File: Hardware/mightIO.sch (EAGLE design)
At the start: 45 parts, among them IC1 TL064D, IC2 TL064D, IC3 LM4041A12DBZ, U1 MAX11612

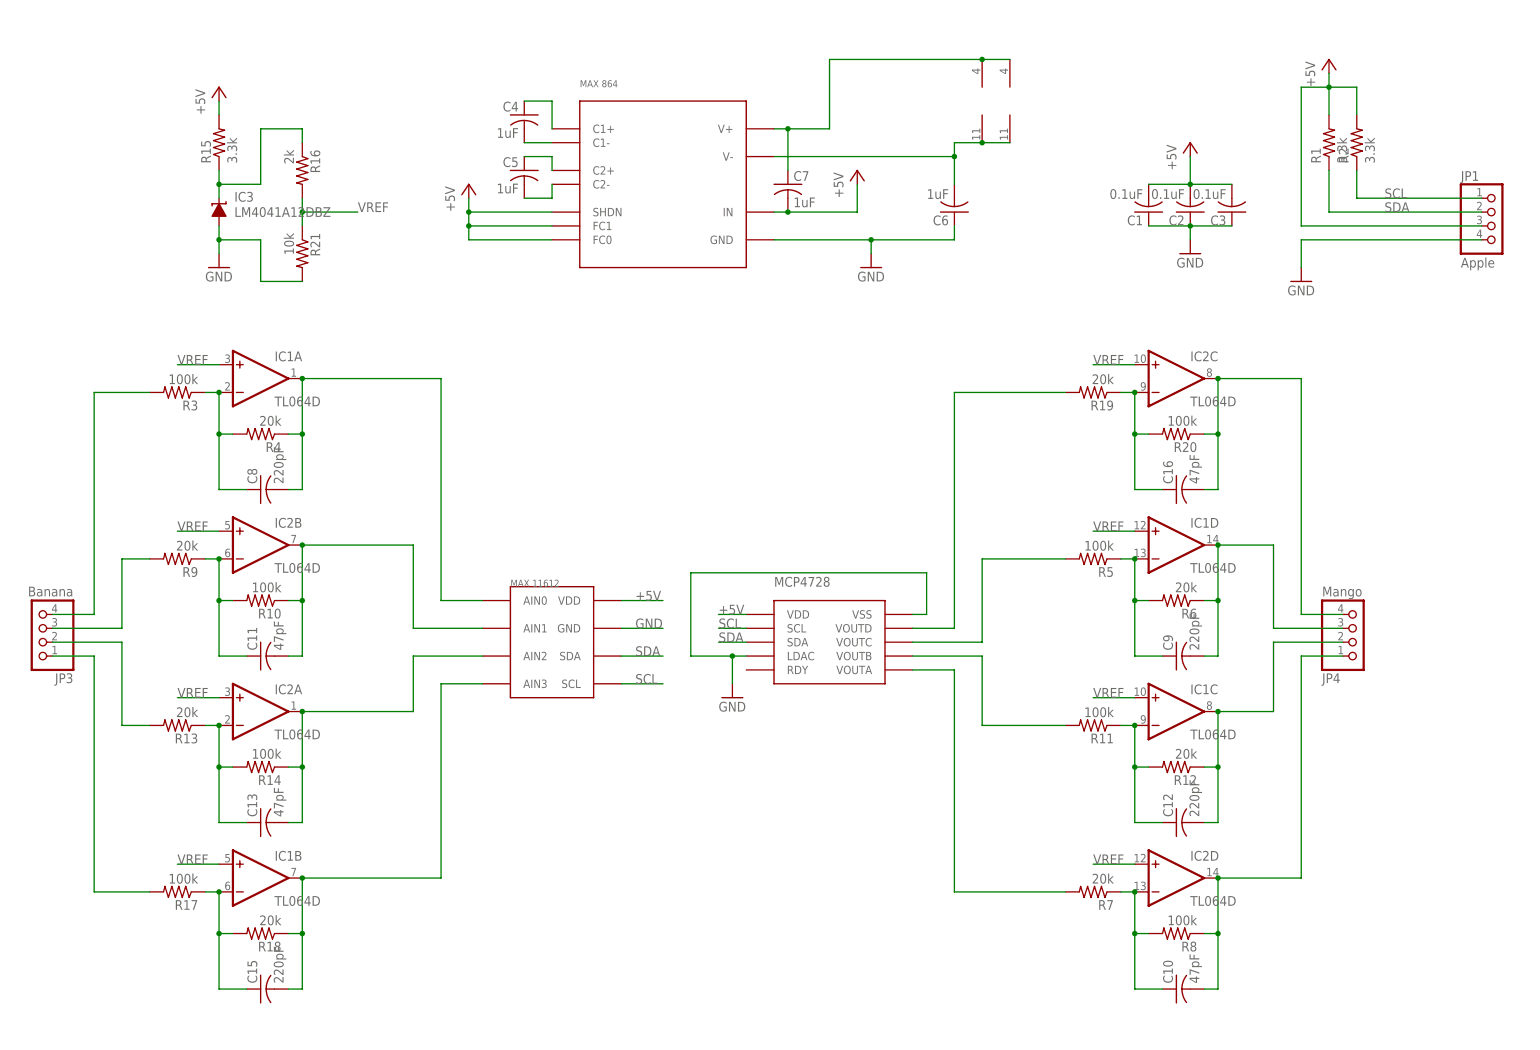
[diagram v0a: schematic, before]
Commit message: Some part value updates
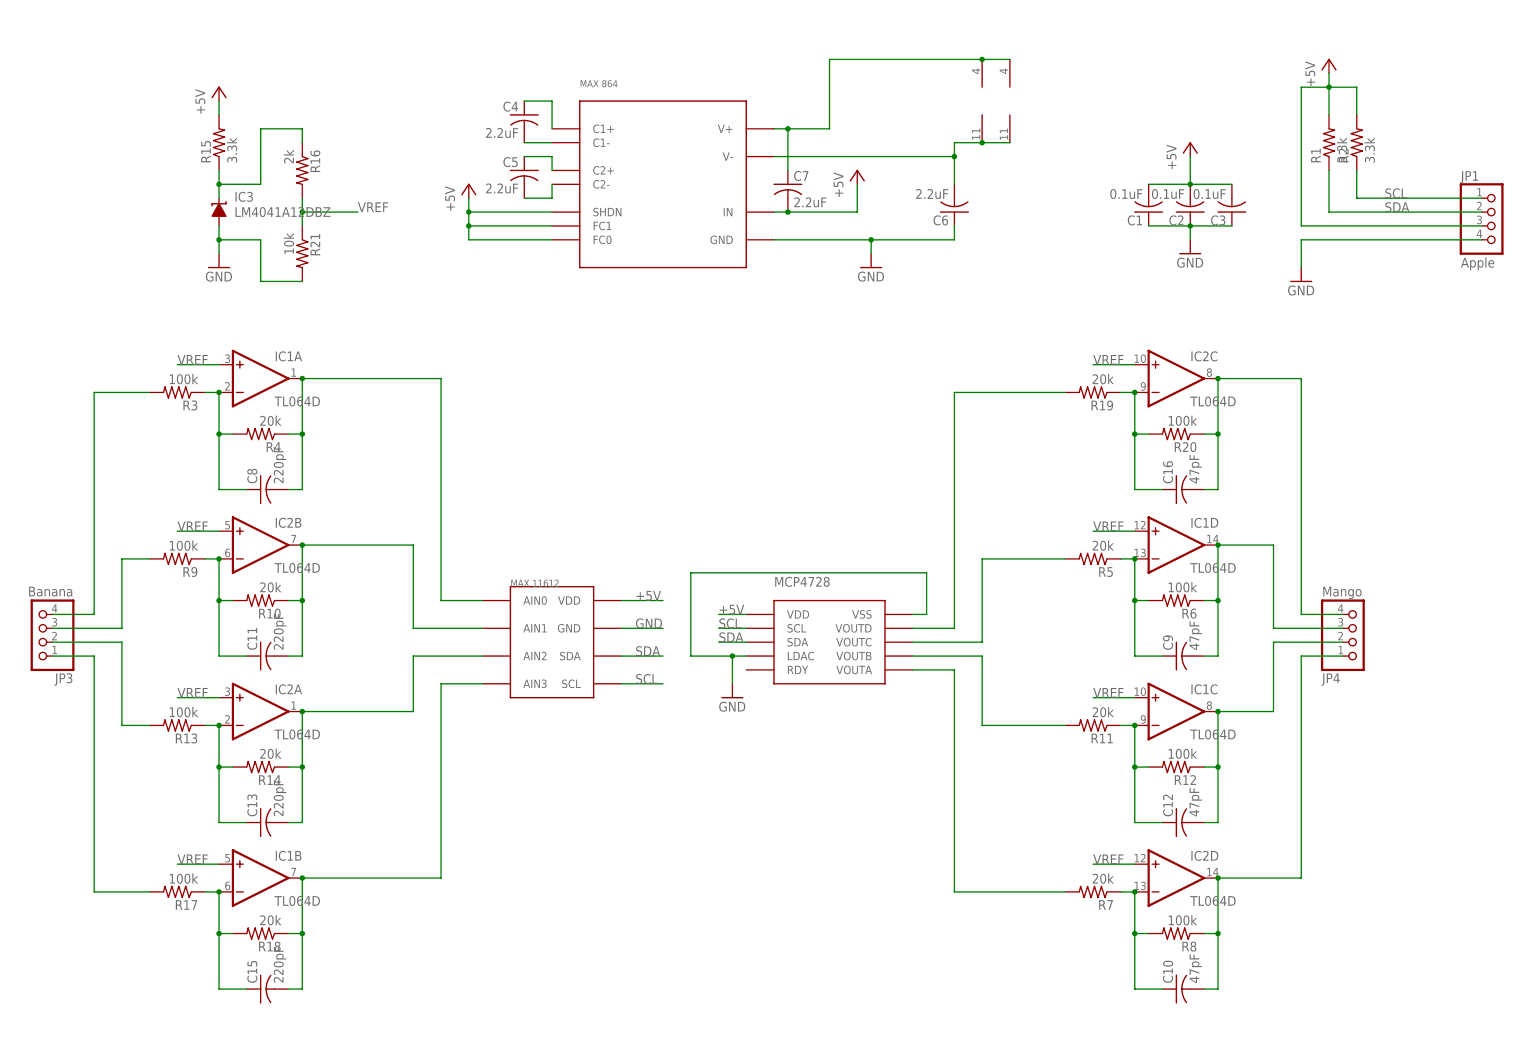
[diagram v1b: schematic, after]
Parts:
- C11, C13: value 47pF -> 220pF
- C12, C9: value 220pF -> 47pF
- C4, C5, C6, C7: value 1uF -> 2.2uF
- R10, R11, R14, R5: value 100k -> 20k
- R12, R13, R6, R9: value 20k -> 100k
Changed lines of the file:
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@@
 <part name="C2" library="rcl" deviceset="C-US" device="C0603" value="0.1uF"/>
 <part name="C3" library="rcl" deviceset="C-US" device="C0603" value="0.1uF"/>
-<part name="C4" library="rcl" deviceset="C-US" device="C0603" value="1uF"/>
-<part name="C5" library="rcl" deviceset="C-US" device="C0603" value="1uF"/>
-<part name="C7" library="rcl" deviceset="C-US" device="C0603" value="1uF"/>
+<part name="C4" library="rcl" deviceset="C-US" device="C0603" value="2.2uF"/>
+<part name="C5" library="rcl" deviceset="C-US" device="C0603" value="2.2uF"/>
+<part name="C7" library="rcl" deviceset="C-US" device="C0603" value="2.2uF"/>
 <part name="P+3" library="supply1" deviceset="+5V" device=""/>
 <part name="P+4" library="supply1" deviceset="+5V" device=""/>
-<part name="C6" library="rcl" deviceset="C-US" device="C0603" value="1uF"/>
+<part name="C6" library="rcl" deviceset="C-US" device="C0603" value="2.2uF"/>
 <part name="IC1" library="linear" deviceset="TL064" device="D"/>
 <part name="IC2" library="linear" deviceset="TL064" device="D"/>
@@
 <part name="R4" library="rcl" deviceset="R-US_" device="R0603" value="20k"/>
 <part name="C8" library="rcl" deviceset="C-US" device="C0603" value="220pF"/>
-<part name="R5" library="rcl" deviceset="R-US_" device="R0603" value="100k"/>
-<part name="R6" library="rcl" deviceset="R-US_" device="R0603" value="20k"/>
-<part name="C9" library="rcl" deviceset="C-US" device="C0603" value="220pF"/>
+<part name="R5" library="rcl" deviceset="R-US_" device="R0603" value="20k"/>
+<part name="R6" library="rcl" deviceset="R-US_" device="R0603" value="100k"/>
+<part name="C9" library="rcl" deviceset="C-US" device="C0603" value="47pF"/>
 <part name="R7" library="rcl" deviceset="R-US_" device="R0603" value="20k"/>
 <part name="R8" library="rcl" deviceset="R-US_" device="R0603" value="100k"/>
 <part name="C10" library="rcl" deviceset="C-US" device="C0603" value="47pF"/>
-<part name="R9" library="rcl" deviceset="R-US_" device="R0603" value="20k"/>
-<part name="R10" library="rcl" deviceset="R-US_" device="R0603" value="100k"/>
-<part name="C11" library="rcl" deviceset="C-US" device="C0603" value="47pF"/>
-<part name="R11" library="rcl" deviceset="R-US_" device="R0603" value="100k"/>
-<part name="R12" library="rcl" deviceset="R-US_" device="R0603" value="20k"/>
-<part name="C12" library="rcl" deviceset="C-US" device="C0603" value="220pF"/>
-<part name="R13" library="rcl" deviceset="R-US_" device="R0603" value="20k"/>
-<part name="R14" library="rcl" deviceset="R-US_" device="R0603" value="100k"/>
-<part name="C13" library="rcl" deviceset="C-US" device="C0603" value="47pF"/>
+<part name="R9" library="rcl" deviceset="R-US_" device="R0603" value="100k"/>
+<part name="R10" library="rcl" deviceset="R-US_" device="R0603" value="20k"/>
+<part name="C11" library="rcl" deviceset="C-US" device="C0603" value="220pF"/>
+<part name="R11" library="rcl" deviceset="R-US_" device="R0603" value="20k"/>
+<part name="R12" library="rcl" deviceset="R-US_" device="R0603" value="100k"/>
+<part name="C12" library="rcl" deviceset="C-US" device="C0603" value="47pF"/>
+<part name="R13" library="rcl" deviceset="R-US_" device="R0603" value="100k"/>
+<part name="R14" library="rcl" deviceset="R-US_" device="R0603" value="20k"/>
+<part name="C13" library="rcl" deviceset="C-US" device="C0603" value="220pF"/>
 <part name="R17" library="rcl" deviceset="R-US_" device="R0603" value="100k"/>
 <part name="R18" library="rcl" deviceset="R-US_" device="R0603" value="20k"/>

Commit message: Some routing updates, more needed
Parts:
- added C14: 0.1uF, rcl:C-USC0603
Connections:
- net GND: now also C14.1
- net VREF: now also C14.2
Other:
- moved on the sheet: IC3, R15, R16, R21
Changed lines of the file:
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@@
 <?xml version="1.0" encoding="utf-8"?>
 <!DOCTYPE eagle SYSTEM "eagle.dtd">
-<eagle version="6.5.0">
+<eagle version="7.0.0">
 <drawing>
 <settings>
@@
 <part name="GND3" library="supply1" deviceset="GND" device=""/>
 <part name="P+1" library="supply1" deviceset="+5V" device=""/>
+<part name="C14" library="rcl" deviceset="C-US" device="C0603" value="0.1uF"/>
 </parts>
 <sheets>
@@
 <instance part="R20" gate="G$1" x="127" y="27.94" rot="R180"/>
 <instance part="C16" gate="G$1" x="127" y="17.78" rot="R90"/>
-<instance part="IC3" gate="G$1" x="-48.26" y="68.58"/>
-<instance part="R15" gate="G$1" x="-48.26" y="81.28" rot="R90"/>
-<instance part="R16" gate="G$1" x="-33.02" y="76.2" rot="R270"/>
-<instance part="R21" gate="G$1" x="-33.02" y="60.96" rot="R270"/>
-<instance part="P+5" gate="1" x="-48.26" y="91.44"/>
-<instance part="GND4" gate="1" x="-48.26" y="58.42"/>
+<instance part="IC3" gate="G$1" x="-63.5" y="71.12"/>
+<instance part="R15" gate="G$1" x="-63.5" y="83.82" rot="R90"/>
+<instance part="R16" gate="G$1" x="-48.26" y="78.74" rot="R270"/>
+<instance part="R21" gate="G$1" x="-48.26" y="63.5" rot="R270"/>
+<instance part="P+5" gate="1" x="-63.5" y="93.98"/>
+<instance part="GND4" gate="1" x="-63.5" y="60.96"/>
 <instance part="JP1" gate="A" x="185.42" y="66.04"/>
 <instance part="GND5" gate="1" x="149.86" y="55.88"/>
@@
 <instance part="GND3" gate="1" x="71.12" y="58.42"/>
 <instance part="P+1" gate="1" x="68.58" y="76.2"/>
+<instance part="C14" gate="G$1" x="-35.56" y="63.5" rot="R180"/>
 </instances>
 <busses>
@@
 <segment>
 <pinref part="IC3" gate="G$1" pin="A"/>
-<wire x1="-48.26" y1="66.04" x2="-48.26" y2="63.5" width="0.1524" layer="91"/>
+<wire x1="-63.5" y1="68.58" x2="-63.5" y2="66.04" width="0.1524" layer="91"/>
 <pinref part="GND4" gate="1" pin="GND"/>
 <pinref part="R21" gate="G$1" pin="2"/>
-<wire x1="-48.26" y1="63.5" x2="-48.26" y2="60.96" width="0.1524" layer="91"/>
-<wire x1="-33.02" y1="55.88" x2="-40.64" y2="55.88" width="0.1524" layer="91"/>
-<wire x1="-40.64" y1="55.88" x2="-40.64" y2="63.5" width="0.1524" layer="91"/>
-<wire x1="-40.64" y1="63.5" x2="-48.26" y2="63.5" width="0.1524" layer="91"/>
-<junction x="-48.26" y="63.5"/>
+<wire x1="-63.5" y1="66.04" x2="-63.5" y2="63.5" width="0.1524" layer="91"/>
+<wire x1="-48.26" y1="58.42" x2="-55.88" y2="58.42" width="0.1524" layer="91"/>
+<wire x1="-55.88" y1="58.42" x2="-55.88" y2="66.04" width="0.1524" layer="91"/>
+<wire x1="-55.88" y1="66.04" x2="-63.5" y2="66.04" width="0.1524" layer="91"/>
+<junction x="-63.5" y="66.04"/>
+<pinref part="C14" gate="G$1" pin="1"/>
+<wire x1="-35.56" y1="60.96" x2="-35.56" y2="58.42" width="0.1524" layer="91"/>
+<wire x1="-35.56" y1="58.42" x2="-48.26" y2="58.42" width="0.1524" layer="91"/>
+<junction x="-48.26" y="58.42"/>
 </segment>
 <segment>
@@
 <pinref part="R15" gate="G$1" pin="2"/>
 <pinref part="P+5" gate="1" pin="+5V"/>
-<wire x1="-48.26" y1="88.9" x2="-48.26" y2="86.36" width="0.1524" layer="91"/>
+<wire x1="-63.5" y1="91.44" x2="-63.5" y2="88.9" width="0.1524" layer="91"/>
 </segment>
 <segment>
@@
 <segment>
 <pinref part="R16" gate="G$1" pin="1"/>
-<wire x1="-33.02" y1="81.28" x2="-33.02" y2="83.82" width="0.1524" layer="91"/>
-<wire x1="-33.02" y1="83.82" x2="-40.64" y2="83.82" width="0.1524" layer="91"/>
-<wire x1="-40.64" y1="83.82" x2="-40.64" y2="73.66" width="0.1524" layer="91"/>
+<wire x1="-48.26" y1="83.82" x2="-48.26" y2="86.36" width="0.1524" layer="91"/>
+<wire x1="-48.26" y1="86.36" x2="-55.88" y2="86.36" width="0.1524" layer="91"/>
+<wire x1="-55.88" y1="86.36" x2="-55.88" y2="76.2" width="0.1524" layer="91"/>
 <pinref part="IC3" gate="G$1" pin="C"/>
-<wire x1="-48.26" y1="71.12" x2="-48.26" y2="73.66" width="0.1524" layer="91"/>
+<wire x1="-63.5" y1="73.66" x2="-63.5" y2="76.2" width="0.1524" layer="91"/>
 <pinref part="R15" gate="G$1" pin="1"/>
-<wire x1="-48.26" y1="73.66" x2="-48.26" y2="76.2" width="0.1524" layer="91"/>
-<wire x1="-40.64" y1="73.66" x2="-48.26" y2="73.66" width="0.1524" layer="91"/>
-<junction x="-48.26" y="73.66"/>
+<wire x1="-63.5" y1="76.2" x2="-63.5" y2="78.74" width="0.1524" layer="91"/>
+<wire x1="-55.88" y1="76.2" x2="-63.5" y2="76.2" width="0.1524" layer="91"/>
+<junction x="-63.5" y="76.2"/>
 </segment>
 </net>
@@
 <pinref part="R21" gate="G$1" pin="1"/>
 <pinref part="R16" gate="G$1" pin="2"/>
-<wire x1="-33.02" y1="66.04" x2="-33.02" y2="68.58" width="0.1524" layer="91"/>
-<wire x1="-33.02" y1="68.58" x2="-33.02" y2="71.12" width="0.1524" layer="91"/>
-<wire x1="-22.86" y1="68.58" x2="-33.02" y2="68.58" width="0.1524" layer="91"/>
-<junction x="-33.02" y="68.58"/>
-<label x="-22.86" y="68.58" size="1.778" layer="95"/>
-</segment>
-<segment>
+<wire x1="-48.26" y1="68.58" x2="-48.26" y2="71.12" width="0.1524" layer="91"/>
+<wire x1="-48.26" y1="71.12" x2="-48.26" y2="73.66" width="0.1524" layer="91"/>
+<wire x1="-30.48" y1="71.12" x2="-35.56" y2="71.12" width="0.1524" layer="91"/>
+<junction x="-48.26" y="71.12"/>
+<label x="-30.48" y="71.12" size="1.778" layer="95"/>
+<pinref part="C14" gate="G$1" pin="2"/>
+<wire x1="-35.56" y1="71.12" x2="-48.26" y2="71.12" width="0.1524" layer="91"/>
+<wire x1="-35.56" y1="68.58" x2="-35.56" y2="71.12" width="0.1524" layer="91"/>
+<junction x="-35.56" y="71.12"/>
+</segment>
+<segment>

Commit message: Layout tweaks, added cap
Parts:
- added C17: 10uF, rcl:CPOL-USE2.5-6
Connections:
- net +5V: now also C17.+
- net GND: now also C17.-
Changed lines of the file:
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@@
 <?xml version="1.0" encoding="utf-8"?>
 <!DOCTYPE eagle SYSTEM "eagle.dtd">
-<eagle version="7.0.0">
+<eagle version="6.5.0">
 <drawing>
 <settings>
@@
 <part name="P+1" library="supply1" deviceset="+5V" device=""/>
 <part name="C14" library="rcl" deviceset="C-US" device="C0603" value="0.1uF"/>
+<part name="C17" library="rcl" deviceset="CPOL-US" device="E2.5-6" value="10uF"/>
 </parts>
 <sheets>
@@
 <instance part="P+1" gate="1" x="68.58" y="76.2"/>
 <instance part="C14" gate="G$1" x="-35.56" y="63.5" rot="R180"/>
+<instance part="C17" gate="G$1" x="111.76" y="71.12" rot="MR0"/>
 </instances>
 <busses>
@@
 <pinref part="C1" gate="G$1" pin="1"/>
 <wire x1="121.92" y1="66.04" x2="129.54" y2="66.04" width="0.1524" layer="91"/>
+<junction x="121.92" y="66.04"/>
+<pinref part="C17" gate="G$1" pin="-"/>
+<wire x1="111.76" y1="66.04" x2="121.92" y2="66.04" width="0.1524" layer="91"/>
 </segment>
 <segment>
@@
 <pinref part="C1" gate="G$1" pin="2"/>
 <wire x1="121.92" y1="73.66" x2="129.54" y2="73.66" width="0.1524" layer="91"/>
-</segment>
-<segment>
+<junction x="121.92" y="73.66"/>
+<pinref part="C17" gate="G$1" pin="+"/>
+<wire x1="111.76" y1="73.66" x2="121.92" y2="73.66" width="0.1524" layer="91"/>
+</segment>
+<segment>

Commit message: Added silkscreen, ready to go
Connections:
- net N$13 renamed AI0
- net N$14 renamed AOB
- net N$16 renamed AI2
- net N$2 renamed AOD
- net N$24 renamed AOA
- net N$30 renamed AOC
- net N$5 renamed AI1
- net N$6 renamed AI3
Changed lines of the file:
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@@
 <?xml version="1.0" encoding="utf-8"?>
 <!DOCTYPE eagle SYSTEM "eagle.dtd">
-<eagle version="6.5.0">
+<eagle version="7.0.0">
 <drawing>
 <settings>
@@
 </segment>
 </net>
-<net name="N$5" class="0">
+<net name="AI1" class="0">
 <segment>
 <wire x1="-66.04" y1="5.08" x2="-66.04" y2="-7.62" width="0.1524" layer="91"/>
@@
 </segment>
 </net>
-<net name="N$13" class="0">
+<net name="AI0" class="0">
 <segment>
 <pinref part="R3" gate="G$1" pin="2"/>
@@
 </segment>
 </net>
-<net name="N$24" class="0">
+<net name="AOA" class="0">
 <segment>
 <pinref part="IC2" gate="D" pin="OUT"/>
@@
 </segment>
 </net>
-<net name="N$6" class="0">
+<net name="AI3" class="0">
 <segment>
 <pinref part="JP3" gate="A" pin="1"/>
@@
 </segment>
 </net>
-<net name="N$30" class="0">
+<net name="AOC" class="0">
 <segment>
 <pinref part="IC1" gate="D" pin="OUT"/>
@@
 </segment>
 </net>
-<net name="N$2" class="0">
+<net name="AOD" class="0">
 <segment>
 <pinref part="IC2" gate="C" pin="OUT"/>
@@
 </segment>
 </net>
-<net name="N$16" class="0">
+<net name="AI2" class="0">
 <segment>
 <pinref part="R13" gate="G$1" pin="2"/>
@@
 </segment>
 </net>
-<net name="N$14" class="0">
+<net name="AOB" class="0">
 <segment>
 <pinref part="IC1" gate="C" pin="OUT"/>
